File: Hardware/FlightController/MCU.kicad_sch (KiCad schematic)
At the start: 22 parts, among them SW1 SW_SPDT, U1 STM32F405RGT6, U4 USBLC6-2SC6, Y1 16MHz

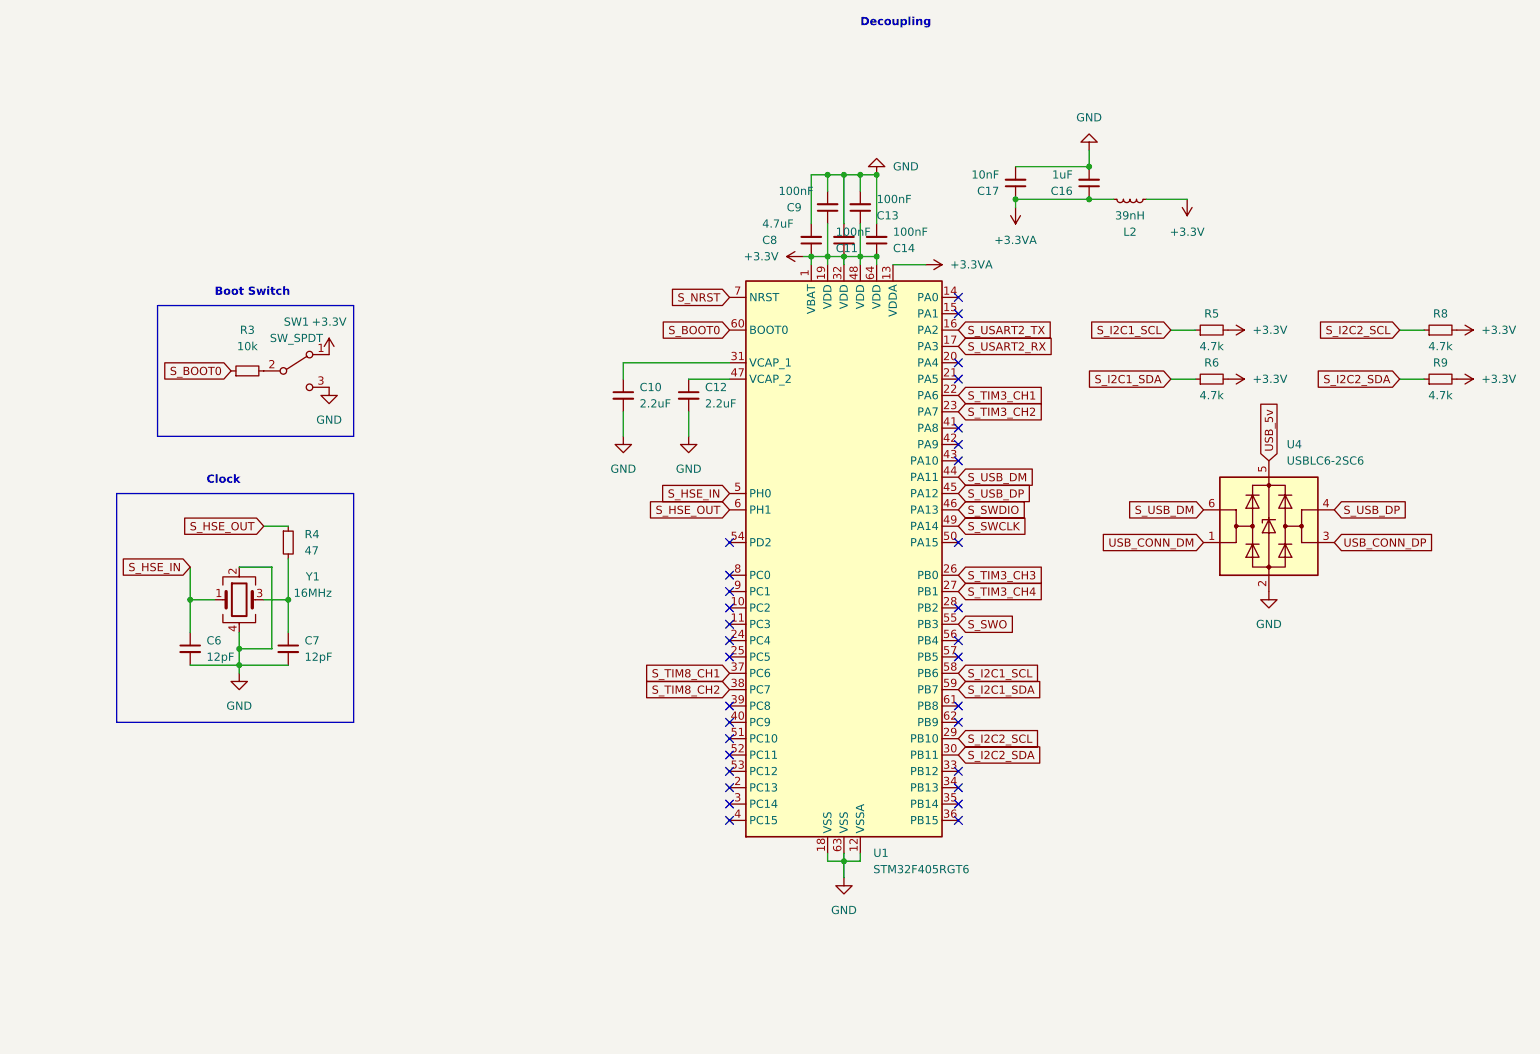
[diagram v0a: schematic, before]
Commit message: Add and route SBUS inverter
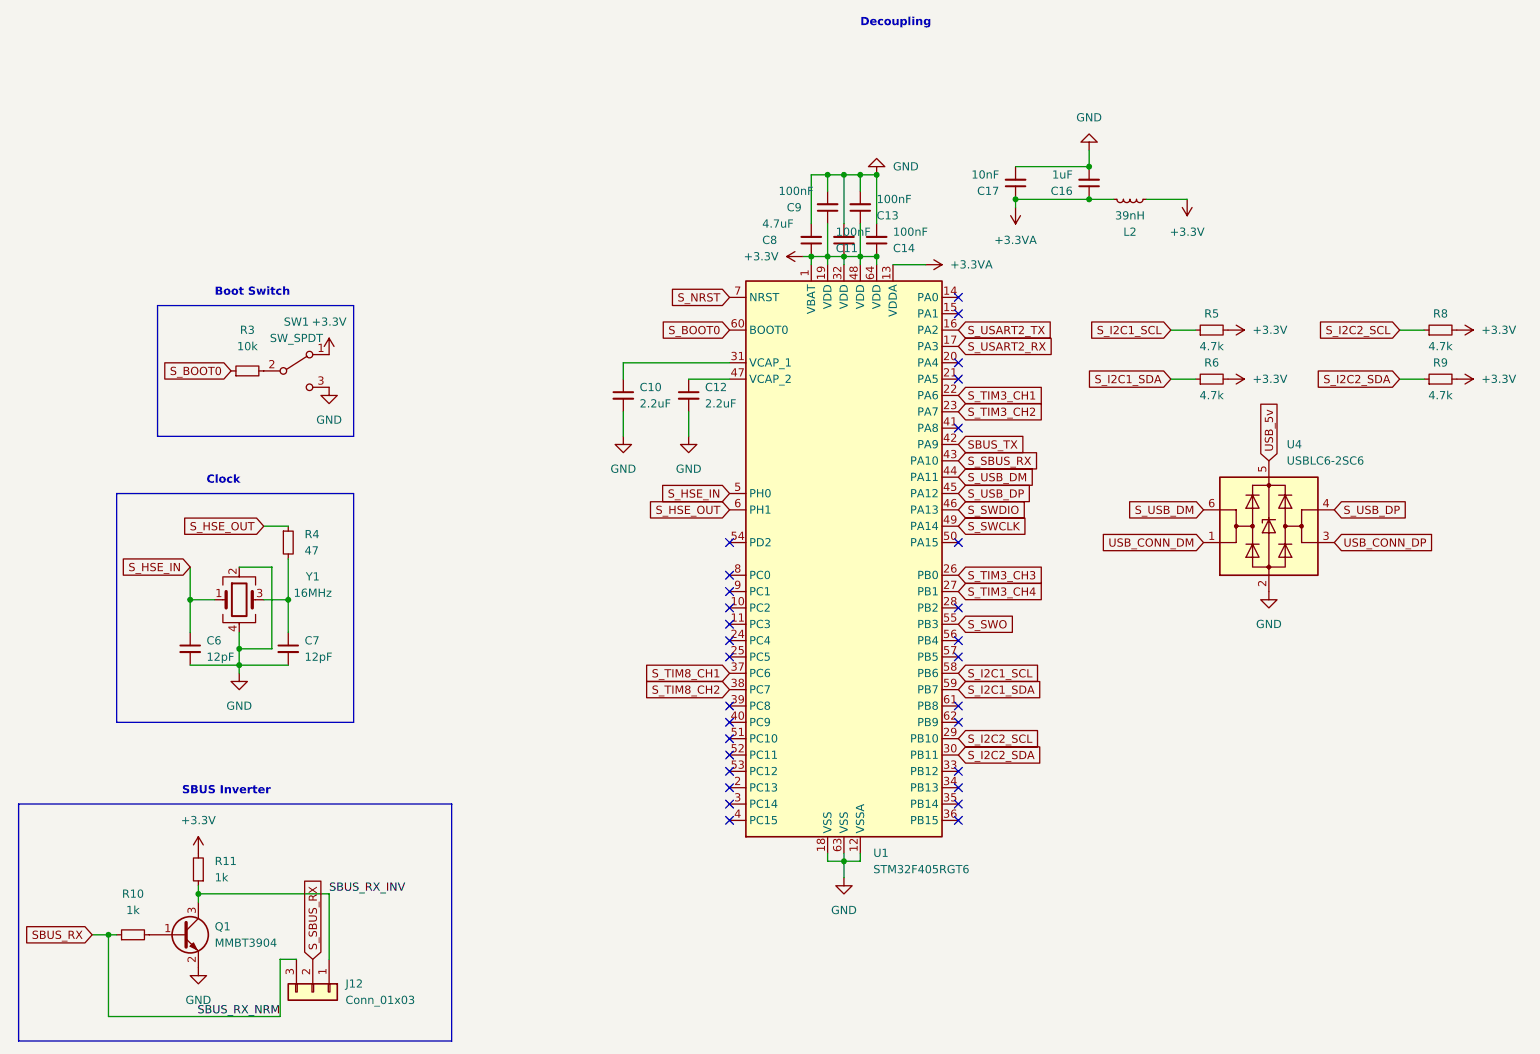
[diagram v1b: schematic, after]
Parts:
- added J12: Conn_01x03, Connector_PinHeader_2.54mm:PinHeader_1x03_P2.54mm_Vertical, symbol Connector_Generic:Conn_01x03
- added Q1: MMBT3904, Package_TO_SOT_SMD:SOT-23, symbol Transistor_BJT:MMBT3904
- added R10, R11: 1k, Resistor_SMD:R_0402_1005Metric, symbol Device:R_Small
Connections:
- net +3V3: now also R11.2
- net GND: now also Q1.2 (E)
- net SBUS_TX: now reaches U1.42 (PA9)
- net S_SBUS_RX: now reaches U1.43 (PA10)
- net S_SBUS_RX: now also J12.2 (Pin_2)
- new net: Q1.1 (B), R10.2
- new net SBUS_RX: J12.3 (Pin_3), R10.1
- new net SBUS_RX_INV: J12.1 (Pin_1), Q1.3 (C), R11.1
- no-connect marks 32 -> 30
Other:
- note added: "SBUS Inverter"

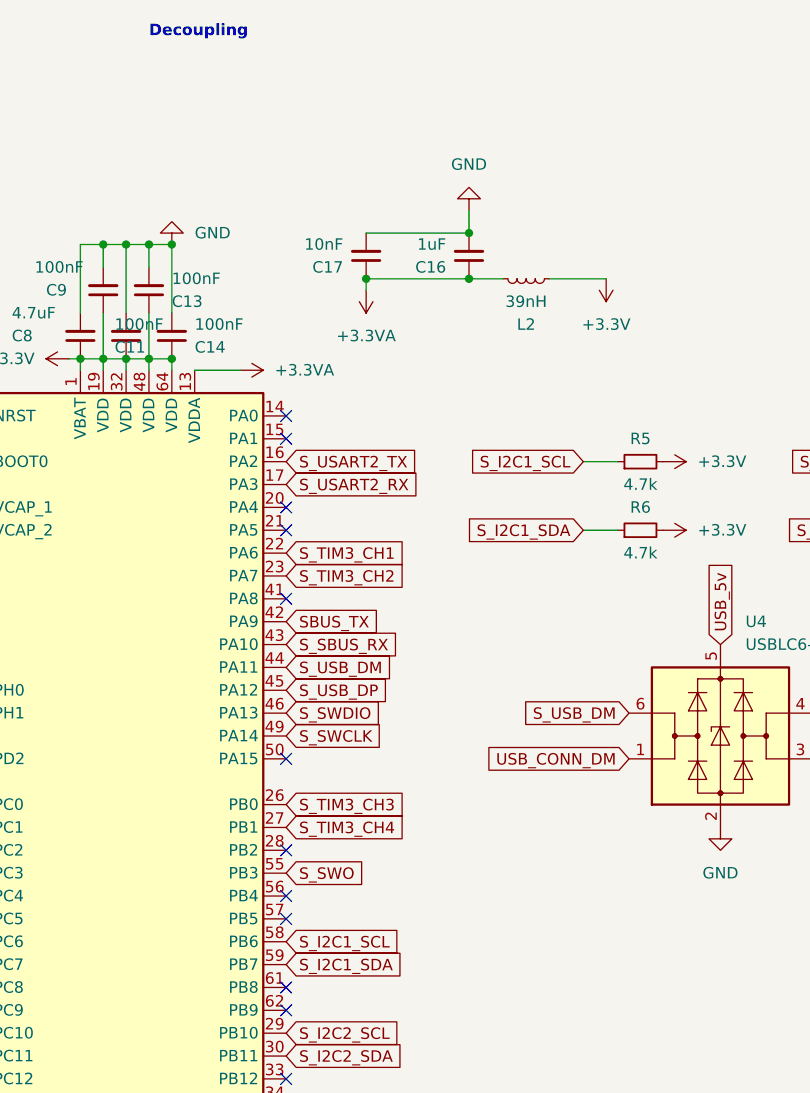
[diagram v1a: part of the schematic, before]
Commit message: Update footprints to be digikey compliant
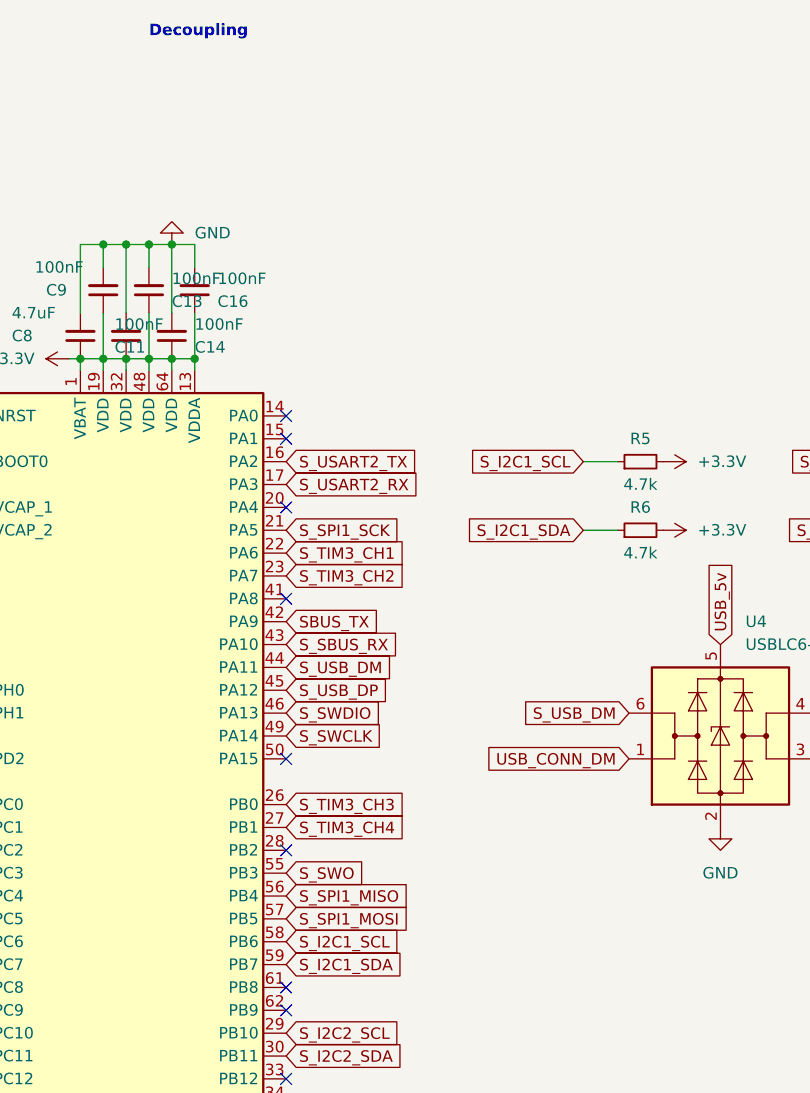
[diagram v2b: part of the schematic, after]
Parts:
- removed C17: 10nF, Capacitor_SMD:C_0402_1005Metric, symbol Device:C_Small
- removed L2: 39nH, Inductor_SMD:L_0402_1005Metric, symbol Device:L_Small
- C16: value 1uF -> 100nF
- SW1: footprint Button_Switch_THT:SW_Slide_1P2T_CK_OS102011MS2Q -> digikey-footprints:Switch_Slide_11.6x4mm_EG1218
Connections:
- net +3.3VA is gone; now on net +3V3: C16.1, U1.13 (VDDA)
- net S_SPI1_SCK: now reaches U1.21 (PA5)
- net S_SPI1_MISO: now reaches U1.56 (PB4)
- net S_SPI1_MOSI: now reaches U1.57 (PB5)
- no-connect marks 30 -> 27

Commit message: Update footprints, routing and LCSC numbers
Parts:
- added U3: W25Q128JVS, Package_SO:SOIC-8_5.23x5.23mm_P1.27mm, symbol Memory_Flash:W25Q128JVS
- C1: renamed from C6; LCSC (none) -> C1547
- C10: renamed from C16; LCSC (none) -> C1525
- C2: renamed from C7; LCSC (none) -> C1547
- C3: renamed from C10; LCSC (none) -> C12530
- C4: renamed from C12; LCSC (none) -> C12530
- C5: renamed from C8; footprint Capacitor_SMD:C_0402_1005Metric -> Capacitor_SMD:C_0603_1608Metric; LCSC (none) -> C19666
- C6: renamed from C9; LCSC (none) -> C1525
- C7: renamed from C11; LCSC (none) -> C1525
- C8: renamed from C13; LCSC (none) -> C1525
- C9: renamed from C14; LCSC (none) -> C1525
- Q1: LCSC (none) -> C20526
- R1: renamed from R10; footprint Resistor_SMD:R_0402_1005Metric -> Resistor_SMD:R_0603_1608Metric; LCSC (none) -> C21190
- R2: renamed from R11; footprint Resistor_SMD:R_0402_1005Metric -> Resistor_SMD:R_0603_1608Metric; LCSC (none) -> C21190
- R3: footprint Resistor_SMD:R_0402_1005Metric -> Resistor_SMD:R_0603_1608Metric; LCSC (none) -> C25804
- R4: LCSC (none) -> C25118
- R5, R6: LCSC (none) -> C25900
- R7: renamed from R8; LCSC (none) -> C25900
- R8: renamed from R9; LCSC (none) -> C25900
- SW1: dk (none) -> y
- U1: LCSC (none) -> C15742
- U2: renamed from U4; LCSC (none) -> C2827654
- Y1: LCSC (none) -> C13738
- renumbered J12 to J1
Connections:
- net +3V3: now also U3.8 (VCC)
- net GND: now also U3.4 (GND)
- net S_SPI1_MISO: now also U3.2 (DO(IO1))
- net S_SPI1_MOSI: now also U3.5 (DI(IO0))
- net S_SPI1_SCK: now also U3.6 (CLK)
- net S_SPI1_CS: now reaches U1.61 (PB8)
- net S_SPI1_CS: now also U3.1 (~{CS})
- net SBUS_RX_INV: no longer names the net of J1.1 (Pin_1), Q1.3 (C), R2.1
- no-connect marks 27 -> 28

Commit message: Finalize design and routing for v1.0 fab
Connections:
- net S_USB_DM renamed S_USB_D-
- net S_USB_DP renamed S_USB_D+
- net USB_CONN_DM renamed USB_CONN_D-
- net USB_CONN_DP renamed USB_CONN_D+
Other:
- note added: "EEPROM"
- note removed: "Decoupling"
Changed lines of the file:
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@@
+    (stroke (width 0) (type default) (color 0 0 0 0))
+  )
+  (polyline (pts (xy 256.54 121.92) (xy 256.54 153.67))
     (stroke (width 0) (type default) (color 0 0 0 0))
   )
@@
     (stroke (width 0) (type default) (color 0 0 0 0))
   )
+  (polyline (pts (xy 198.12 121.92) (xy 256.54 121.92))
+    (stroke (width 0) (type default) (color 0 0 0 0))
+  )
   (wire (pts (xy 153.67 153.67) (xy 153.67 154.94))
     (stroke (width 0) (type default) (color 0 0 0 0))
@@
     (stroke (width 0) (type default) (color 0 0 0 0))
   )
+  (polyline (pts (xy 198.12 153.67) (xy 198.12 121.92))
+    (stroke (width 0) (type default) (color 0 0 0 0))
+  )
   (wire (pts (xy 52.07 114.3) (xy 52.07 119.38))
     (stroke (width 0) (type default) (color 0 0 0 0))
@@
   )
   (wire (pts (xy 161.29 55.88) (xy 161.29 60.96))
+    (stroke (width 0) (type default) (color 0 0 0 0))
+  )
+  (polyline (pts (xy 256.54 153.67) (xy 198.12 153.67))
     (stroke (width 0) (type default) (color 0 0 0 0))
   )
@@
     (effects (font (size 1.27 1.27) bold) (justify left bottom))
   )
-  (text "Decoupling" (at 156.21 25.4 0)
+  (text "EEPROM" (at 224.79 120.65 0)
     (effects (font (size 1.27 1.27) bold) (justify left bottom))
   )
@@
     )
   )
-  (global_label "USB_CONN_DP" (shape input) (at 229.87 105.41 0) (fields_autoplaced)
-    (effects (font (size 1.27 1.27)) (justify left))
-    (property "Intersheet References" "${INTERSHEET_REFS}" (id 0) (at 245.8298 105.3306 0)
+  (global_label "USB_CONN_D+" (shape input) (at 229.87 105.41 0) (fields_autoplaced)
+    (effects (font (size 1.27 1.27)) (justify left))
+    (property "Intersheet References" "${INTERSHEET_REFS}" (id 0) (at 246.1321 105.3306 0)
       (effects (font (size 1.27 1.27)) (justify left) hide)
     )
@@
     )
   )
-  (global_label "S_USB_DP" (shape input) (at 229.87 100.33 0) (fields_autoplaced)
-    (effects (font (size 1.27 1.27)) (justify left))
-    (property "Intersheet References" "${INTERSHEET_REFS}" (id 0) (at 241.7779 100.2506 0)
-      (effects (font (size 1.27 1.27)) (justify left) hide)
-    )
-  )
-  (global_label "S_USB_DP" (shape input) (at 171.45 97.79 0) (fields_autoplaced)
-    (effects (font (size 1.27 1.27)) (justify left))
-    (property "Intersheet References" "${INTERSHEET_REFS}" (id 0) (at 183.3579 97.7106 0)
+  (global_label "S_USB_D+" (shape input) (at 229.87 100.33 0) (fields_autoplaced)
+    (effects (font (size 1.27 1.27)) (justify left))
+    (property "Intersheet References" "${INTERSHEET_REFS}" (id 0) (at 242.0802 100.2506 0)
+      (effects (font (size 1.27 1.27)) (justify left) hide)
+    )
+  )
+  (global_label "S_USB_D+" (shape input) (at 171.45 97.79 0) (fields_autoplaced)
+    (effects (font (size 1.27 1.27)) (justify left))
+    (property "Intersheet References" "${INTERSHEET_REFS}" (id 0) (at 183.6602 97.7106 0)
       (effects (font (size 1.27 1.27)) (justify left) hide)
     )
@@
     )
   )
-  (global_label "USB_CONN_DM" (shape input) (at 209.55 105.41 180) (fields_autoplaced)
-    (effects (font (size 1.27 1.27)) (justify right))
-    (property "Intersheet References" "${INTERSHEET_REFS}" (id 0) (at 193.4088 105.3306 0)
+  (global_label "USB_CONN_D-" (shape input) (at 209.55 105.41 180) (fields_autoplaced)
+    (effects (font (size 1.27 1.27)) (justify right))
+    (property "Intersheet References" "${INTERSHEET_REFS}" (id 0) (at 193.2879 105.3306 0)
       (effects (font (size 1.27 1.27)) (justify right) hide)
     )
@@
     )
   )
-  (global_label "S_USB_DM" (shape input) (at 209.55 100.33 180) (fields_autoplaced)
-    (effects (font (size 1.27 1.27)) (justify right))
-    (property "Intersheet References" "${INTERSHEET_REFS}" (id 0) (at 197.4607 100.4094 0)
+  (global_label "S_USB_D-" (shape input) (at 209.55 100.33 180) (fields_autoplaced)
+    (effects (font (size 1.27 1.27)) (justify right))
+    (property "Intersheet References" "${INTERSHEET_REFS}" (id 0) (at 197.3398 100.2506 0)
       (effects (font (size 1.27 1.27)) (justify right) hide)
     )
@@
     )
   )
-  (global_label "S_USB_DM" (shape input) (at 171.45 95.25 0) (fields_autoplaced)
-    (effects (font (size 1.27 1.27)) (justify left))
-    (property "Intersheet References" "${INTERSHEET_REFS}" (id 0) (at 183.5393 95.1706 0)
-      (effects (font (size 1.27 1.27)) (justify left) hide)
-    )
+  (global_label "S_USB_D-" (shape input) (at 171.45 95.25 0) (fields_autoplaced)
+    (effects (font (size 1.27 1.27)) (justify left))
+    (property "Intersheet References" "${INTERSHEET_REFS}" (id 0) (at 183.6602 95.1706 0)
+      (effects (font (size 1.27 1.27)) (justify left) hide)
+    )
